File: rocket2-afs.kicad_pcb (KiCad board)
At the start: 4 copper layers, 70 x 50 mm, 72 parts, among them J1 ARMING_PLUG, J2 POWER, J3 E-MATCH_DROGUE, J4 SWD, J5 E-MATCH_RECOVERY, Q1 Q_NMOS_GSD, Q2 Q_NMOS_GSD, Q3 Q_NMOS_GSD, Q4 Q_NMOS_GSD, Q5 Q_NMOS_GSD, U2 LD1086DT33TR, U8 USBLC6-2SC6, Y1 16MHz

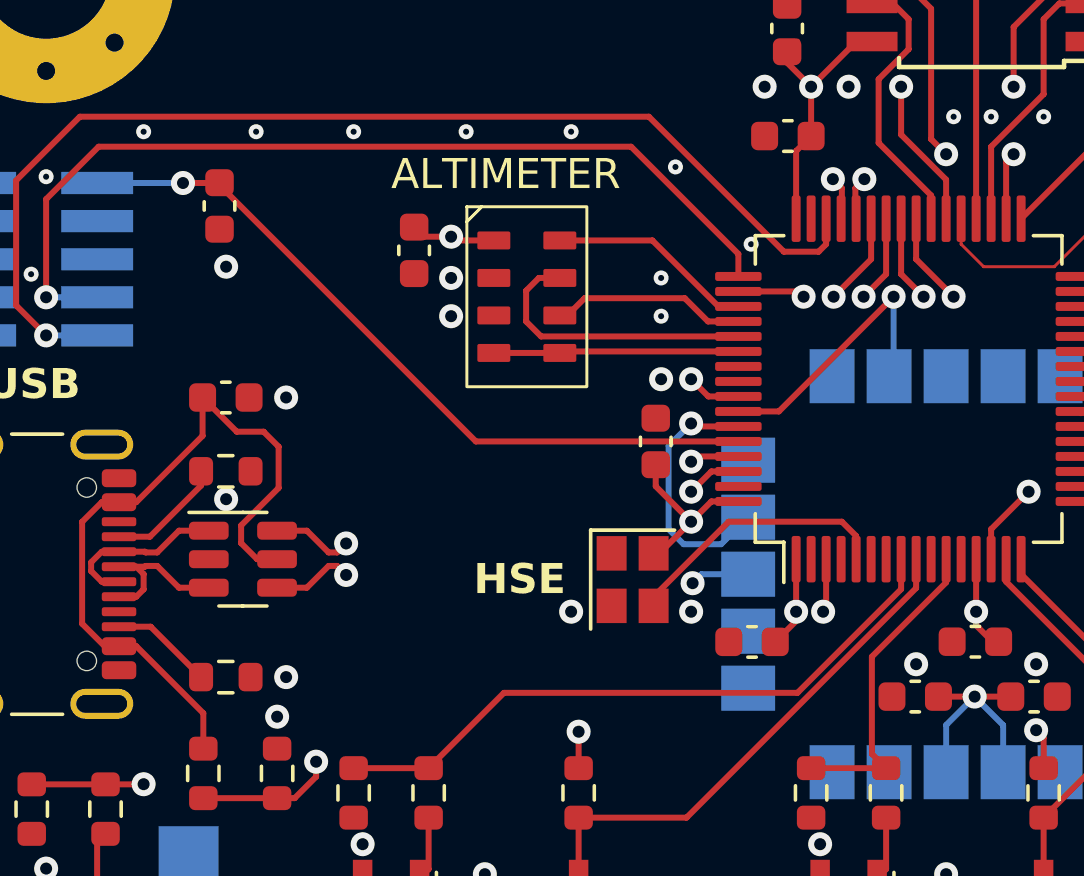
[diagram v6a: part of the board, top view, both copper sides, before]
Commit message: Moved BOOT0 Schematic to RST
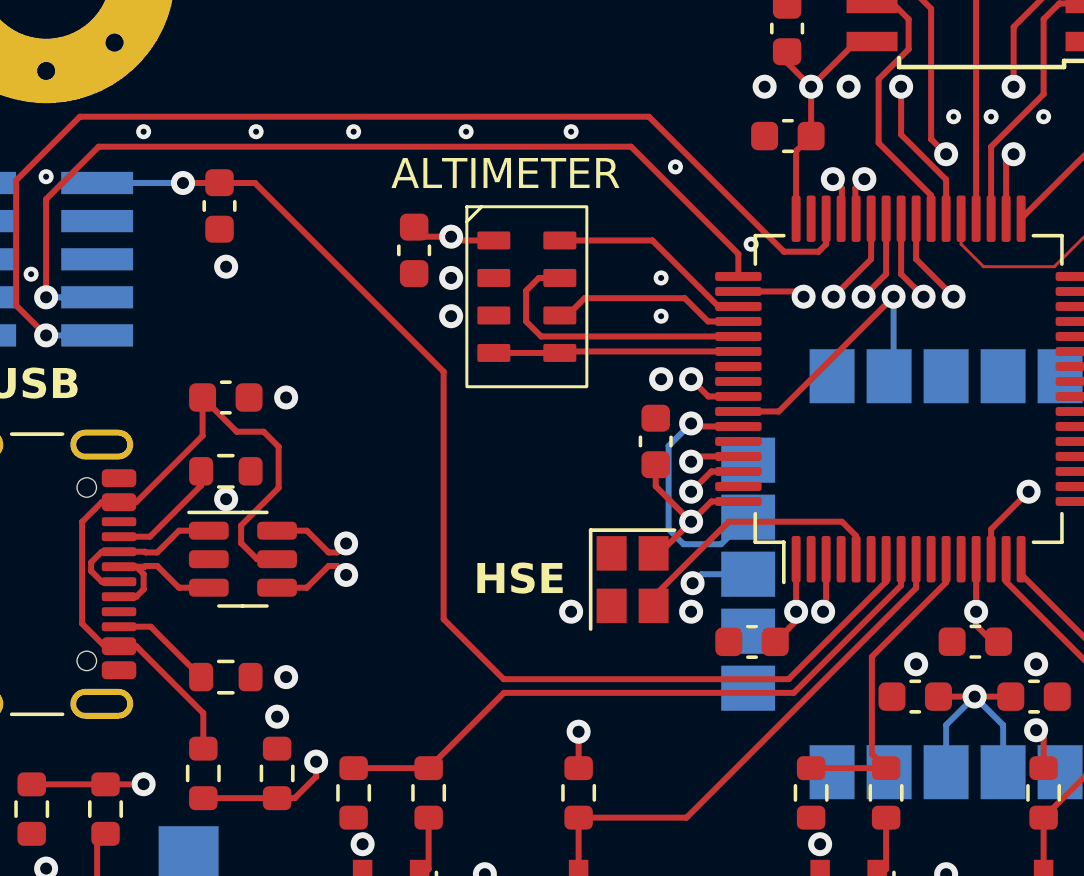
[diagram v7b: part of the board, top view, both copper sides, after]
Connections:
- U1 pad 60: NRST -> GND
- U1 pad 7: GND -> NRST
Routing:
- net NRST: track 26.2 -> 41.3 mm
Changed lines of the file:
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@@
       (net 38 "unconnected-(U1-PD1-Pad6)") (pinfunction "PD1") (pintype "bidirectional+no_connect"))
     (pad "7" smd roundrect (at -5.675 -0.75 90) (size 1.55 0.3) (layers "F.Cu" "F.Paste" "F.Mask") (roundrect_rratio 0.25)
-      (net 1 "GND") (pinfunction "~{RST}") (pintype "input"))
+      (net 2 "NRST") (pinfunction "~{RST}") (pintype "input"))
     (pad "8" smd roundrect (at -5.675 -0.25 90) (size 1.55 0.3) (layers "F.Cu" "F.Paste" "F.Mask") (roundrect_rratio 0.25)
       (net 23 "DROGUE") (pinfunction "PC0") (pintype "bidirectional"))
@@
       (net 34 "GPS_SDA") (pinfunction "PB7") (pintype "bidirectional"))
     (pad "60" smd roundrect (at -1.75 -5.675 90) (size 0.3 1.55) (layers "F.Cu" "F.Paste" "F.Mask") (roundrect_rratio 0.25)
-      (net 2 "NRST") (pinfunction "BOOT0") (pintype "input"))
+      (net 1 "GND") (pinfunction "BOOT0") (pintype "input"))
     (pad "61" smd roundrect (at -2.25 -5.675 90) (size 0.3 1.55) (layers "F.Cu" "F.Paste" "F.Mask") (roundrect_rratio 0.25)
       (net 63 "GPS_RESET") (pinfunction "PB8") (pintype "bidirectional"))
@@
   (via (at 132 70.25) (size 0.5) (drill 0.2) (layers "F.Cu" "B.Cu") (free) (net 1))
   (via (at 187 75) (size 0.8) (drill 0.4) (layers "F.Cu" "B.Cu") (free) (net 1))
-  (segment (start 130.71 71.96) (end 129.5625 71.96) (width 0.2) (layer "F.Cu") (net 2))
-  (segment (start 148.075 80.575) (end 139.325 80.575) (width 0.2) (layer "F.Cu") (net 2))
-  (segment (start 139.325 80.575) (end 130.71 71.96) (width 0.2) (layer "F.Cu") (net 2))
+  (segment (start 138.25 86.5) (end 138.25 78.25) (width 0.2) (layer "F.Cu") (net 2))
+  (segment (start 153 84.5) (end 153 85.25) (width 0.2) (layer "F.Cu") (net 2))
+  (segment (start 131.96 71.96) (end 129.5625 71.96) (width 0.2) (layer "F.Cu") (net 2))
+  (segment (start 140.25 88.5) (end 138.25 86.5) (width 0.2) (layer "F.Cu") (net 2))
+  (segment (start 153 85.25) (end 149.75 88.5) (width 0.2) (layer "F.Cu") (net 2))
+  (segment (start 149.75 88.5) (end 140.25 88.5) (width 0.2) (layer "F.Cu") (net 2))
+  (segment (start 138.25 78.25) (end 131.96 71.96) (width 0.2) (layer "F.Cu") (net 2))
   (via (at 129.5625 71.96) (size 0.8) (drill 0.4) (layers "F.Cu" "B.Cu") (net 2))
   (segment (start 129.75 72) (end 129.71 71.96) (width 0.2) (layer "B.Cu") (net 2))
@@
   (segment (start 154 85.462132) (end 154 84.5) (width 0.2) (layer "F.Cu") (net 22))
   (segment (start 142.75 95.13) (end 142.75 93.115) (width 0.2) (layer "F.Cu") (net 22))
-  (segment (start 153.5 85.5) (end 153.5 84.5) (width 0.2) (layer "F.Cu") (net 23))
-  (segment (start 137.75 91.465) (end 140.26 88.955) (width 0.2) (layer "F.Cu") (net 23))
-  (segment (start 140.26 88.955) (end 150.045 88.955) (width 0.2) (layer "F.Cu") (net 23))
   (segment (start 135.25 91.465) (end 137.75 91.465) (width 0.2) (layer "F.Cu") (net 23))
-  (segment (start 150.045 88.955) (end 153.5 85.5) (width 0.2) (layer "F.Cu") (net 23))
+  (segment (start 149.92 88.955) (end 153.5 85.375) (width 0.2) (layer "F.Cu") (net 23))
+  (segment (start 140.26 88.955) (end 149.92 88.955) (width 0.2) (layer "F.Cu") (net 23))
+  (segment (start 137.75 91.465) (end 140.26 88.955) (width 0.2) (layer "F.Cu") (net 23))
+  (segment (start 153.5 85.375) (end 153.5 84.5) (width 0.2) (layer "F.Cu") (net 23))
   (segment (start 155 85.274999) (end 155 84.5) (width 0.2) (layer "F.Cu") (net 24))
   (segment (start 152.525 87.749999) (end 155 85.274999) (width 0.2) (layer "F.Cu") (net 24))
